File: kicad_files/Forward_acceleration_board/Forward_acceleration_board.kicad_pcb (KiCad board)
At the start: 2 copper layers, 203.2 x 228.6 mm, 0 parts

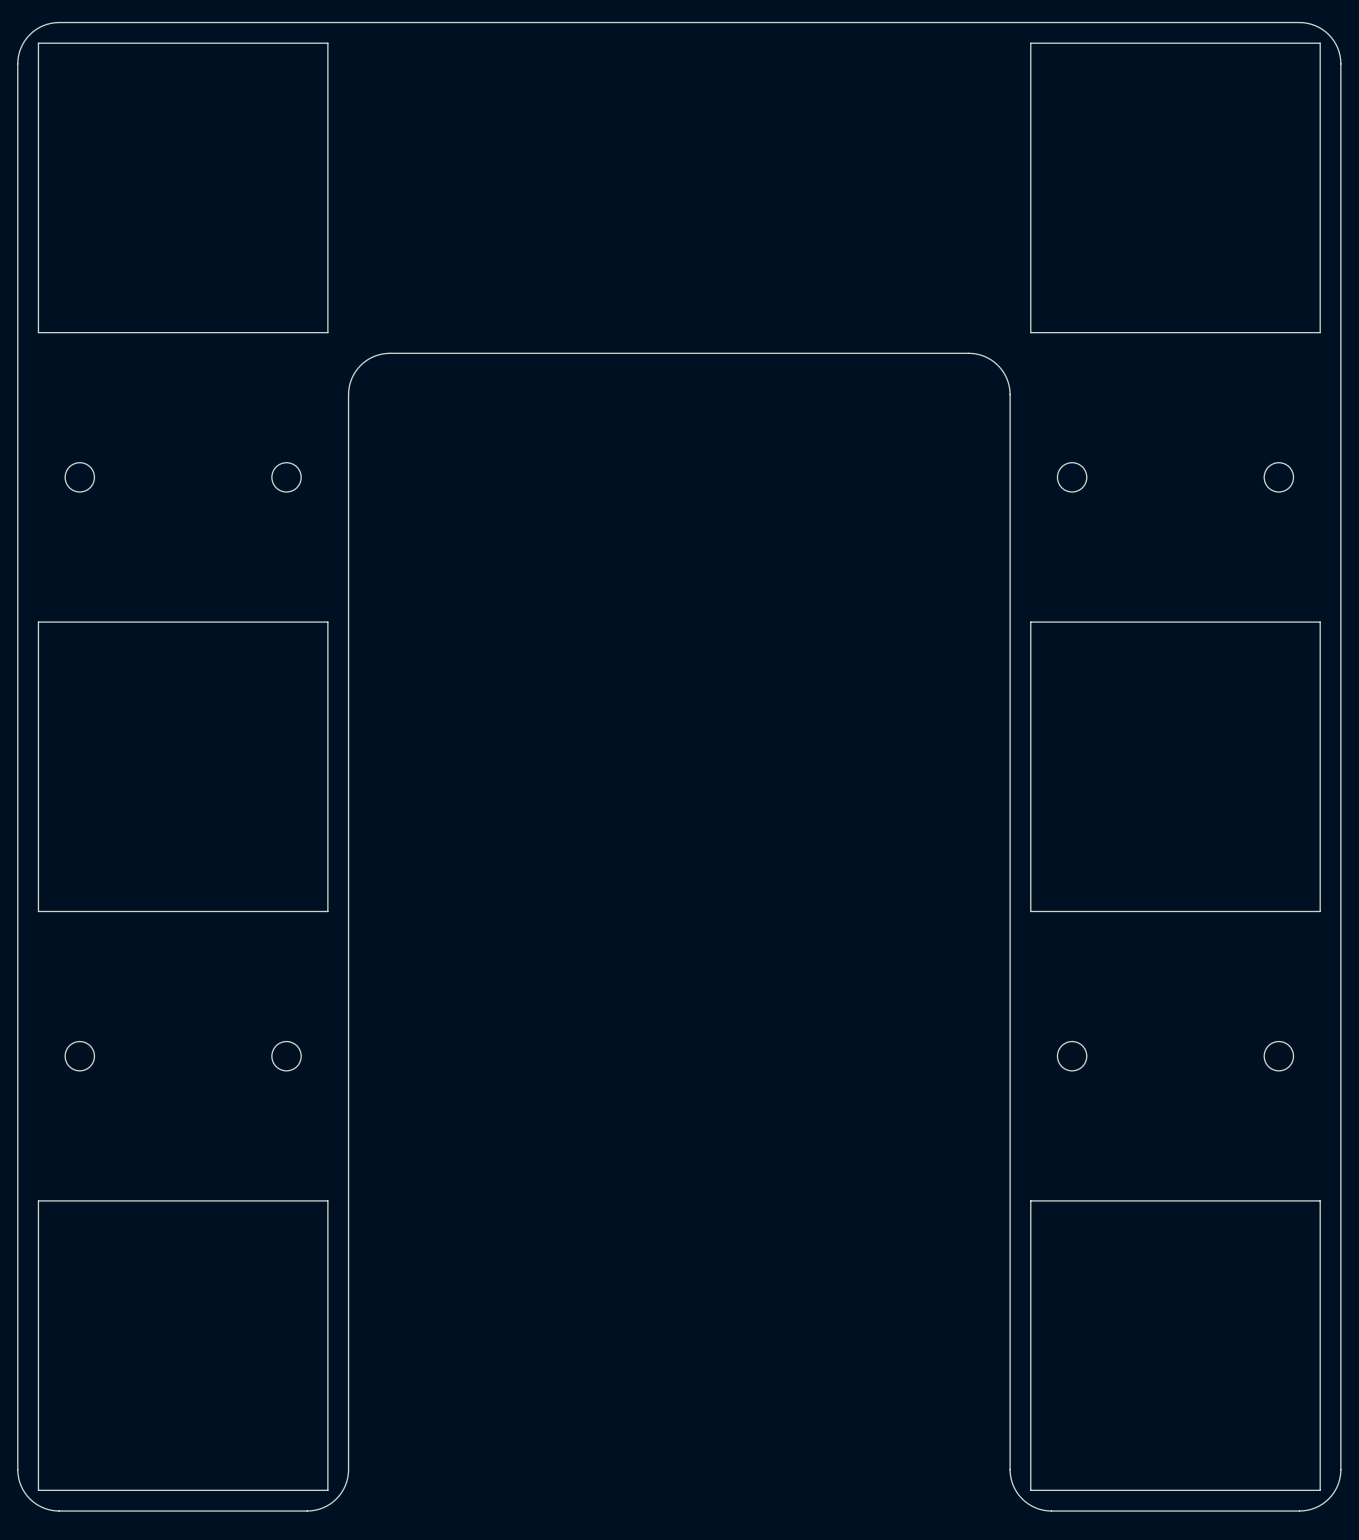
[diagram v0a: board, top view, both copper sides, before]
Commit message: nearly completed forward acceleration control board rounded edges and established clearence for motor control board made progress canabalizing Vedder's code for motor control
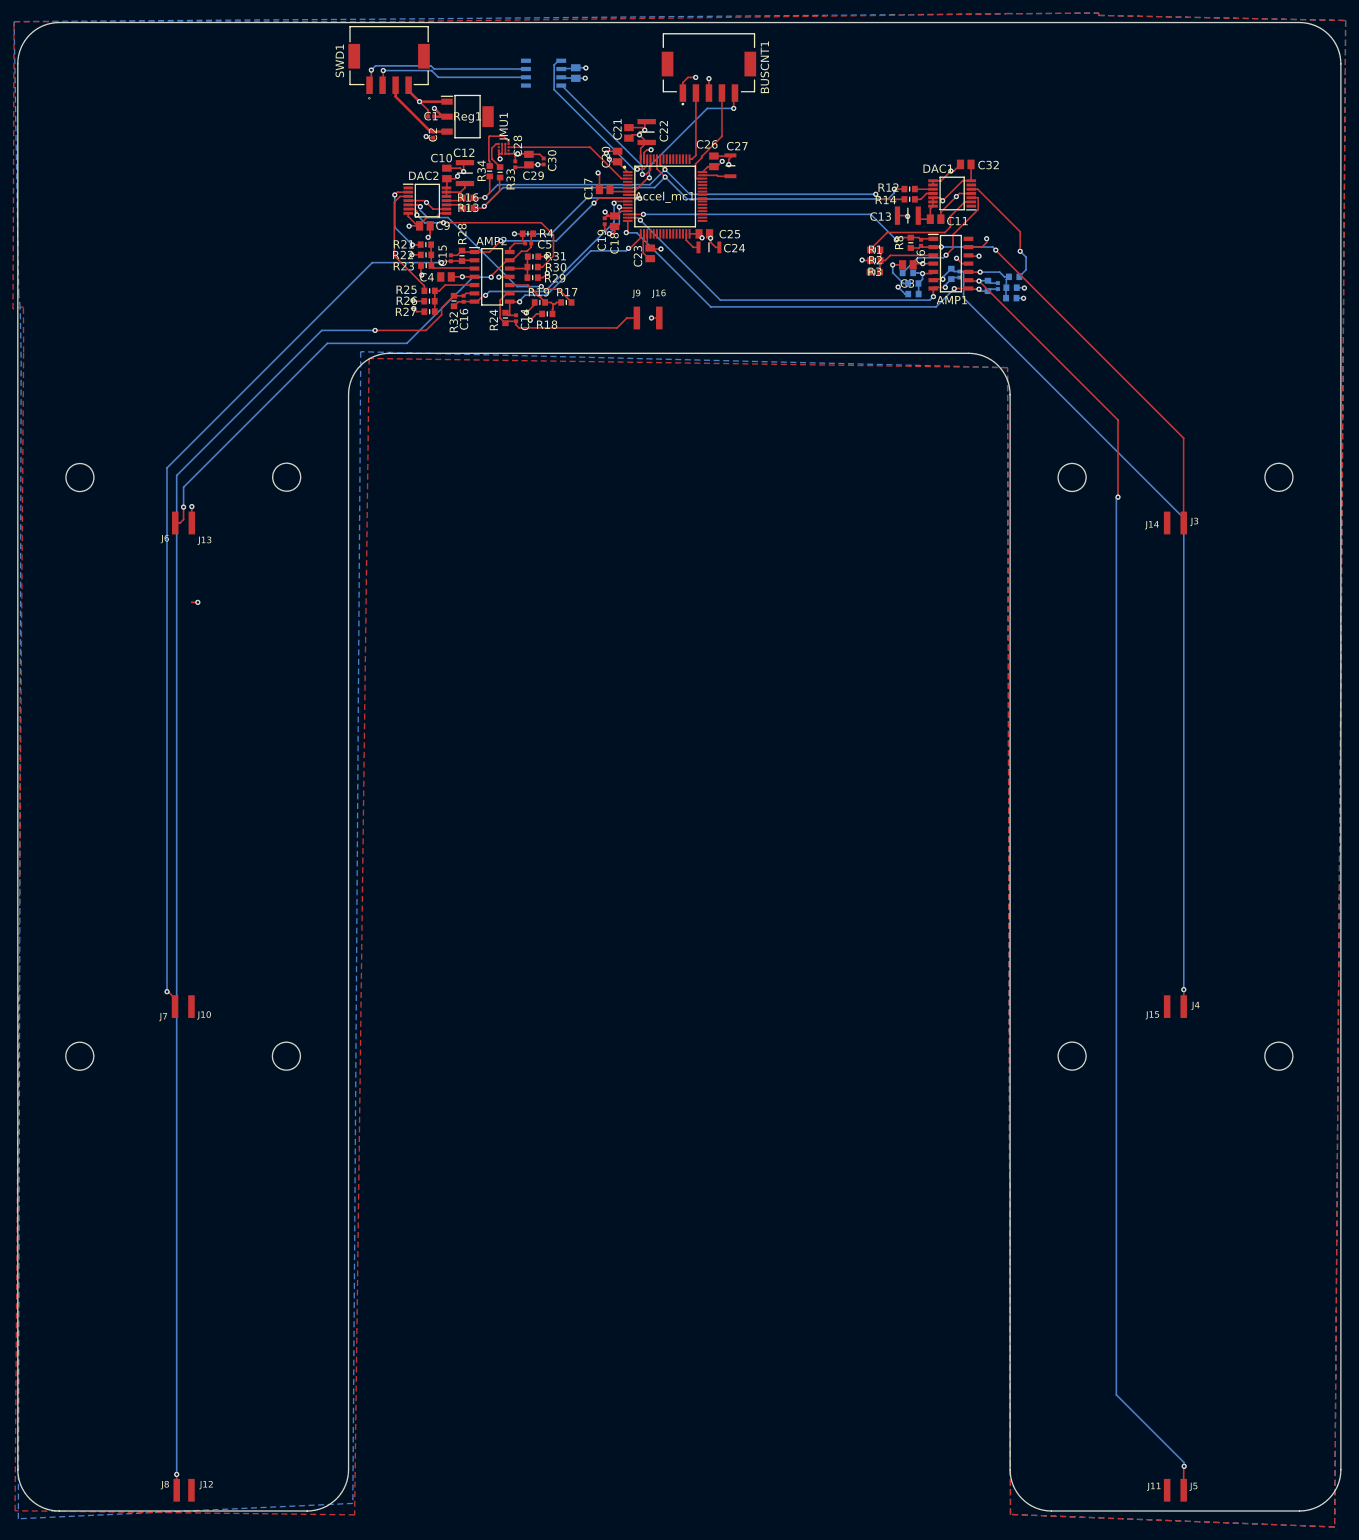
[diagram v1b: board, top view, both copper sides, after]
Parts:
- added AMP1: MCP6054+E_SL, MCP6054-E_SL:SOIC127P600X175-14N, F.Cu at (225.9, 69.3)
- added AMP2: MCP6054+E_SL, MCP6054-E_SL:SOIC127P600X175-14N, F.Cu at (155.4, 71.3)
- added Accel_mc1: STM32F205RBT6, STM32F205RBT6:QFP50P1200X1200X160-64N, F.Cu at (182.0, 59.0)
- added BUSCNT1: SM05B-PASS-TBT(LF)(SN), SM05B-PASS-TBT(LF)(SN):SM05BPASSTBTLFSN, F.Cu at (188.7, 39.5)
- added C1: 1u, GRM155C91C105ME11J:CAPC1005X55N, F.Cu at (146.1, 46.7)
- added C10: .1u, AS0805KKX7R0BB104:CAPC2012X145N, F.Cu at (148.5, 55.5)
- added C11: .1u, AS0805KKX7R0BB104:CAPC2012X145N, F.Cu at (223.5, 62.5)
- added C12: 4.7u, CGA6M3X7S2A475K200AB:CAPC3225X200N, F.Cu at (151.2, 55.4)
- added C13: 4.7u, CGA6M3X7S2A475K200AB:CAPC3225X200N, F.Cu at (219.3, 61.9)
- added C14: 47p, GRM155C91C105ME11J:CAPC1005X55N, F.Cu at (159.1, 77.7)
- added C15: 47p, GRM155C91C105ME11J:CAPC1005X55N, F.Cu at (149.1, 68.5)
- added C16: 47p, GRM155C91C105ME11J:CAPC1005X55N, F.Cu at (151.1, 74.7)
- added C17: .1u, AS0805KKX7R0BB104:CAPC2012X145N, F.Cu at (172.7, 57.9)
- added C18: .1u, AS0805KKX7R0BB104:CAPC2012X145N, F.Cu at (174.2, 62.8)
- added C19: 1u, GRM155C91C105ME11J:CAPC1005X55N, F.Cu at (172.7, 62.8)
- added C2: 1u, GRM155C91C105ME11J:CAPC1005X55N, F.Cu at (146.4, 49.5)
- added C20: .1u, AS0805KKX7R0BB104:CAPC2012X145N, F.Cu at (174.7, 52.9)
- added C21: .1u, AS0805KKX7R0BB104:CAPC2012X145N, F.Cu at (176.4, 49.2)
- added C22: 4.7u, CGA6M3X7S2A475K200AB:CAPC3225X200N, F.Cu at (179.2, 49.1)
- added C23: .1u, AS0805KKX7R0BB104:CAPC2012X145N, F.Cu at (179.7, 67.7)
- added C24: 2.2u, C3216X7R1H225K160AE:CAPC3216X180N, F.Cu at (188.7, 66.8)
- added C25: .1u, AS0805KKX7R0BB104:CAPC2012X145N, F.Cu at (188.0, 64.7)
- added C26: .1u, AS0805KKX7R0BB104:CAPC2012X145N, F.Cu at (189.5, 53.6)
- added C27: 2.2u, C3216X7R1H225K160AE:CAPC3216X180N, F.Cu at (192.0, 54.3)
- added C28: .1u, GRM155C91C105ME11J:CAPC1005X55N, F.Cu at (159.0, 54.0)
- added C29: 10u, AS0805KKX7R0BB104:CAPC2012X145N, F.Cu at (161.1, 53.3)
- added C3: .1u, AS0805KKX7R0BB104:CAPC2012X145N, F.Cu at (219.3, 69.5)
- added C30: .1u, GRM155C91C105ME11J:CAPC1005X55N, F.Cu at (163.3, 53.6)
- added C31: 100n, AS0805KKX7R0BB104:CAPC2012X145N, B.Cu at (168.3, 40.0)
- added C32: .1u, AS0805KKX7R0BB104:CAPC2012X145N, F.Cu at (228.2, 54.1)
- added C4: .1u, AS0805KKX7R0BB104:CAPC2012X145N, F.Cu at (148.3, 71.3)
- added C5: 47p, GRM155C91C105ME11J:CAPC1005X55N, F.Cu at (161.0, 66.2)
- added C6: 47p, GRM155C91C105ME11J:CAPC1005X55N, F.Cu at (221.3, 66.1)
- added C7: 47p, GRM155C91C105ME11J:CAPC1005X55N, B.Cu at (227.2, 71.0)
- added C8: 47p, GRM155C91C105ME11J:CAPC1005X55N, B.Cu at (233.1, 72.8)
- added C9: .1u, AS0805KKX7R0BB104:CAPC2012X145N, F.Cu at (145.1, 63.5)
- added CAN_TR1: SN65HVD232DR, SN65HVD232DR:SOIC127P600X175-8N, B.Cu at (163.3, 40.0)
- added DAC1: MAX5815BAUD+, MAX5815BAUD+:SOP65P640X110-14N, F.Cu at (226.1, 58.5)
- added DAC2: MAX5815BAUD+, MAX5815BAUD+:SOP65P640X110-14N, F.Cu at (145.5, 59.6)
- added IMU1: LIS2DTW12TR, LIS2DTW12TR:IIS2MDCTR, F.Cu at (157.2, 51.7)
- added J10: Conn_01x01_Male, Wire_Pads:SolderWirePad_1x01_SMD_1.27x2.54mm, F.Cu at (109.2, 210.6)
- added J11: Conn_01x01_Male, Wire_Pads:SolderWirePad_1x01_SMD_1.27x2.54mm, F.Cu at (259.1, 257.7)
- added J12: Conn_01x01_Male, Wire_Pads:SolderWirePad_1x01_SMD_1.27x2.54mm, F.Cu at (109.2, 284.8)
- added J13: Conn_01x01_Male, Wire_Pads:SolderWirePad_1x01_SMD_1.27x2.54mm, F.Cu at (109.3, 121.3)
- added J14: Conn_01x01_Male, Wire_Pads:SolderWirePad_1x01_SMD_1.27x2.54mm, F.Cu at (259.1, 109.1)
- added J15: Conn_01x01_Male, Wire_Pads:SolderWirePad_1x01_SMD_1.27x2.54mm, F.Cu at (259.1, 183.4)
- added J16: Conn_01x01_Male, Wire_Pads:SolderWirePad_1x01_SMD_1.27x2.54mm, F.Cu at (181.1, 77.7)
- added J3: Conn_01x01_Male, Wire_Pads:SolderWirePad_1x01_SMD_1.27x2.54mm, F.Cu at (261.6, 109.1)
- added J4: Conn_01x01_Male, Wire_Pads:SolderWirePad_1x01_SMD_1.27x2.54mm, F.Cu at (261.6, 183.4)
- added J5: Conn_01x01_Male, Wire_Pads:SolderWirePad_1x01_SMD_1.27x2.54mm, F.Cu at (261.6, 257.7)
- added J6: Conn_01x01_Male, Wire_Pads:SolderWirePad_1x01_SMD_1.27x2.54mm, F.Cu at (106.8, 121.3)
- added J7: Conn_01x01_Male, Wire_Pads:SolderWirePad_1x01_SMD_1.27x2.54mm, F.Cu at (106.7, 210.5)
- added J8: Conn_01x01_Male, Wire_Pads:SolderWirePad_1x01_SMD_1.27x2.54mm, F.Cu at (67.7, 245.4)
- added J9: Conn_01x01_Male, Wire_Pads:SolderWirePad_1x01_SMD_1.27x2.54mm, F.Cu at (177.7, 77.7)
- added R1: 5k, ERJ3RQF4R7V:RESC1608X55N, F.Cu at (214.3, 67.2)
- added R10: 20k, ERJ3RQF4R7V:RESC1608X55N, B.Cu at (235.2, 74.6)
- added R11: 100k, ERJ3RQF4R7V:RESC1608X55N, B.Cu at (235.2, 73.0)
- added R12: 5k, ERJ3RQF4R7V:RESC1608X55N, F.Cu at (219.6, 57.9)
- added R13: 5k, ERJ3RQF4R7V:RESC1608X55N, F.Cu at (151.8, 60.8)
- added R14: 5k, ERJ3RQF4R7V:RESC1608X55N, F.Cu at (219.6, 59.4)
- added R15: 50k, ERJ3RQF4R7V:RESC1608X55N, B.Cu at (225.9, 70.9)
- added R16: 5k, ERJ3RQF4R7V:RESC1608X55N, F.Cu at (151.7, 59.2)
- added R17: 5k, ERJ3RQF4R7V:RESC1608X55N, F.Cu at (166.8, 75.3)
- added R18: 20k, ERJ3RQF4R7V:RESC1608X55N, F.Cu at (163.9, 77.0)
- added R19: 100k, ERJ3RQF4R7V:RESC1608X55N, F.Cu at (162.8, 75.3)
- added R2: 20k, ERJ3RQF4R7V:RESC1608X55N, F.Cu at (214.3, 68.8)
- added R20: 50k, ERJ3RQF4R7V:RESC1608X55N, B.Cu at (231.6, 72.7)
- added R21: 5k, ERJ3RQF4R7V:RESC1608X55N, F.Cu at (145.2, 66.4)
- added R22: 20k, ERJ3RQF4R7V:RESC1608X55N, F.Cu at (145.3, 68.0)
- added R23: 100k, ERJ3RQF4R7V:RESC1608X55N, F.Cu at (145.3, 69.6)
- added R24: 50k, ERJ3RQF4R7V:RESC1608X55N, F.Cu at (157.5, 77.7)
- added R25: 5k, ERJ3RQF4R7V:RESC1608X55N, F.Cu at (145.8, 73.5)
- added R26: 20k, ERJ3RQF4R7V:RESC1608X55N, F.Cu at (145.8, 75.1)
- added R27: 100k, ERJ3RQF4R7V:RESC1608X55N, F.Cu at (145.8, 76.7)
- added R28: 50k, ERJ3RQF4R7V:RESC1608X55N, F.Cu at (150.8, 68.1)
- added R29: 5k, ERJ3RQF4R7V:RESC1608X55N, F.Cu at (161.7, 71.5)
- added R3: 100k, ERJ3RQF4R7V:RESC1608X55N, F.Cu at (214.2, 70.6)
- added R30: 20k, ERJ3RQF4R7V:RESC1608X55N, F.Cu at (161.7, 69.8)
- added R31: 100k, ERJ3RQF4R7V:RESC1608X55N, F.Cu at (161.7, 68.2)
- added R32: 50k, ERJ3RQF4R7V:RESC1608X55N, F.Cu at (149.6, 75.0)
- added R33: 5k, ERJ3RQF4R7V:RESC1608X55N, F.Cu at (156.7, 55.3)
- added R34: 5k, ERJ3RQF4R7V:RESC1608X55N, F.Cu at (155.1, 55.1)
- added R4: 50k, ERJ3RQF4R7V:RESC1608X55N, F.Cu at (160.9, 64.7)
- added R5: 5k, ERJ3RQF4R7V:RESC1608X55N, B.Cu at (219.3, 70.7)
- added R6: 20k, ERJ3RQF4R7V:RESC1608X55N, B.Cu at (220.1, 74.0)
- added R7: 100k, ERJ3RQF4R7V:RESC1608X55N, B.Cu at (220.1, 72.3)
- added R8: 50k, ERJ3RQF4R7V:RESC1608X55N, F.Cu at (219.7, 66.1)
- added R9: 5k, ERJ3RQF4R7V:RESC1608X55N, B.Cu at (235.6, 71.3)
- added REF**: MountingHole_4.3mm_M4, MountingHole:MountingHole_4.3mm_M4, F.Cu at (276.3, 102.1)
- added REF**: MountingHole_4.3mm_M4, MountingHole:MountingHole_4.3mm_M4, F.Cu at (123.8, 191.0)
- added REF**: MountingHole_4.3mm_M4, MountingHole:MountingHole_4.3mm_M4, F.Cu at (92.1, 102.2)
- added REF**: MountingHole_4.3mm_M4, MountingHole:MountingHole_4.3mm_M4, F.Cu at (244.5, 102.1)
- added REF**: MountingHole_4.3mm_M4, MountingHole:MountingHole_4.3mm_M4, F.Cu at (276.2, 191.0)
- added REF**: MountingHole_4.3mm_M4, MountingHole:MountingHole_4.3mm_M4, F.Cu at (244.5, 191.0)
- added REF**: MountingHole_4.3mm_M4, MountingHole:MountingHole_4.3mm_M4, F.Cu at (92.1, 191.0)
- added REF**: MountingHole_4.3mm_M4, MountingHole:MountingHole_4.3mm_M4, F.Cu at (123.9, 102.1)
- added Reg1: TC2117, TC2117:SOT230P700X180-4N, F.Cu at (151.7, 46.7)
- added SWD1: SM04B-PASS-TBT(LF)(SN), SM04B-PASS-TBT(LF)(SN):SM04B-PASS-TBT, F.Cu at (139.6, 41.8)
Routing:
- net /FSR_Circuitry/-ref6: track 0.00 -> 213.8 mm, vias 0 -> 2
- net /FSR_Circuitry/-ref3: track 0.00 -> 204.0 mm, vias 0 -> 3
- net /FSR_Circuitry/-ref5: track 0.00 -> 143.9 mm, vias 0 -> 2
- net /FSR_Circuitry/-ref2: track 0.00 -> 132.6 mm, vias 0 -> 2
- net GND: track 0.00 -> 110.3 mm, vias 0 -> 32
- net +3V3: track 0.00 -> 102.0 mm, vias 0 -> 23
- net /Controller/SDA: track 0.00 -> 79.4 mm, vias 0 -> 3
- net /FSR_Circuitry/-ref4: track 0.00 -> 77.4 mm, vias 0 -> 2
- net /Controller/SCL: track 0.00 -> 75.7 mm, vias 0 -> 3
- net /FSR_Circuitry/-ref1: track 0.00 -> 67.4 mm, vias 0 -> 2
- net /Controller/Bottom_left_FSR_out: track 0.00 -> 65.2 mm, vias 0 -> 3
- net /FSR_Circuitry/FSR_out2: track 0.00 -> 58.6 mm, vias 0 -> 3
- net /FSR_Circuitry/FSR_out1: track 0.00 -> 49.6 mm, vias 0 -> 2
- net /Controller/Bottom_right_FSR_out: track 0.00 -> 35.1 mm, vias 0 -> 2
- net /FSR_Circuitry/break_DAC: track 0.00 -> 31.7 mm, vias 0 -> 2
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- added copper zone on In1.Cu, net +3V3
- added copper zone on B.Cu, net GND
- added copper zone on F.Cu, net GND
- added copper zone on In2.Cu, net GND
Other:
- outline, holes or cut-outs redrawn
- copper layers 2 -> 4

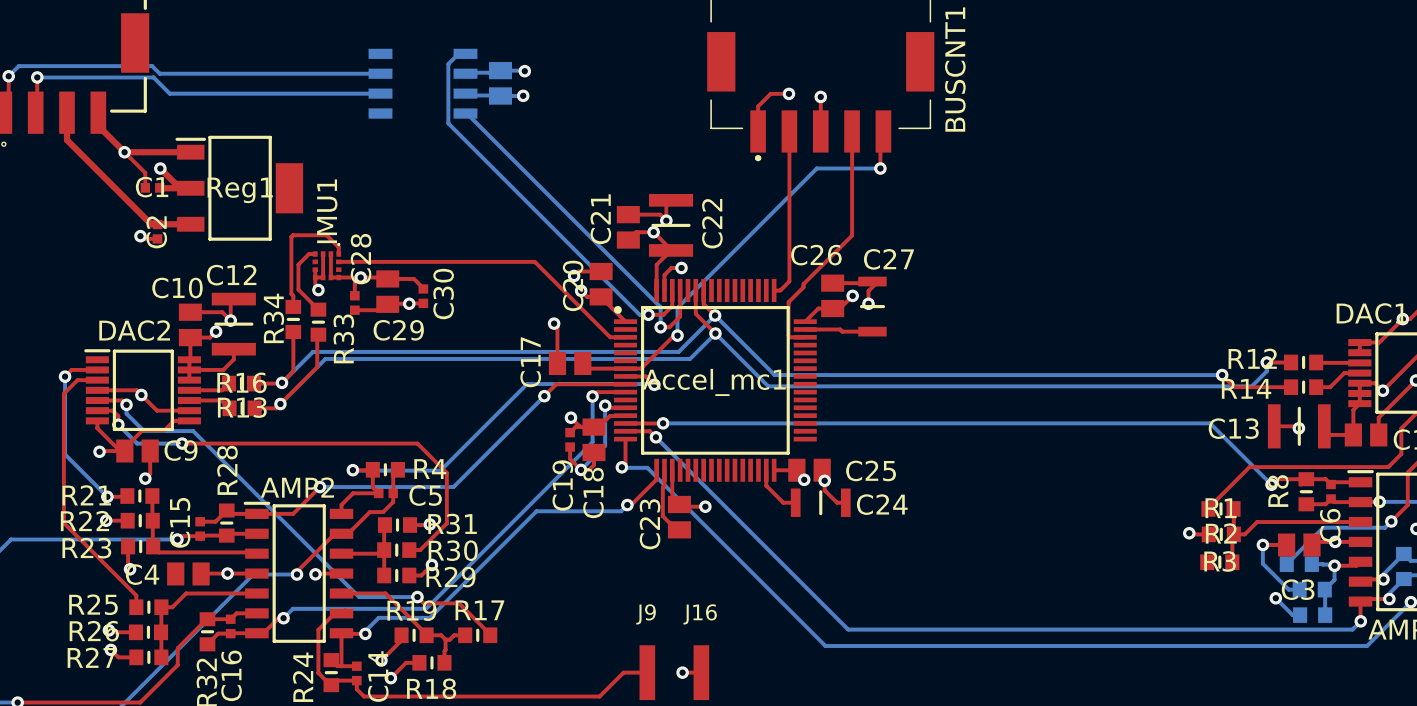
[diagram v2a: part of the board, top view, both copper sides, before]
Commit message: replaced 220nf resistor with component that fit, moved silkscreen around, updated BOM
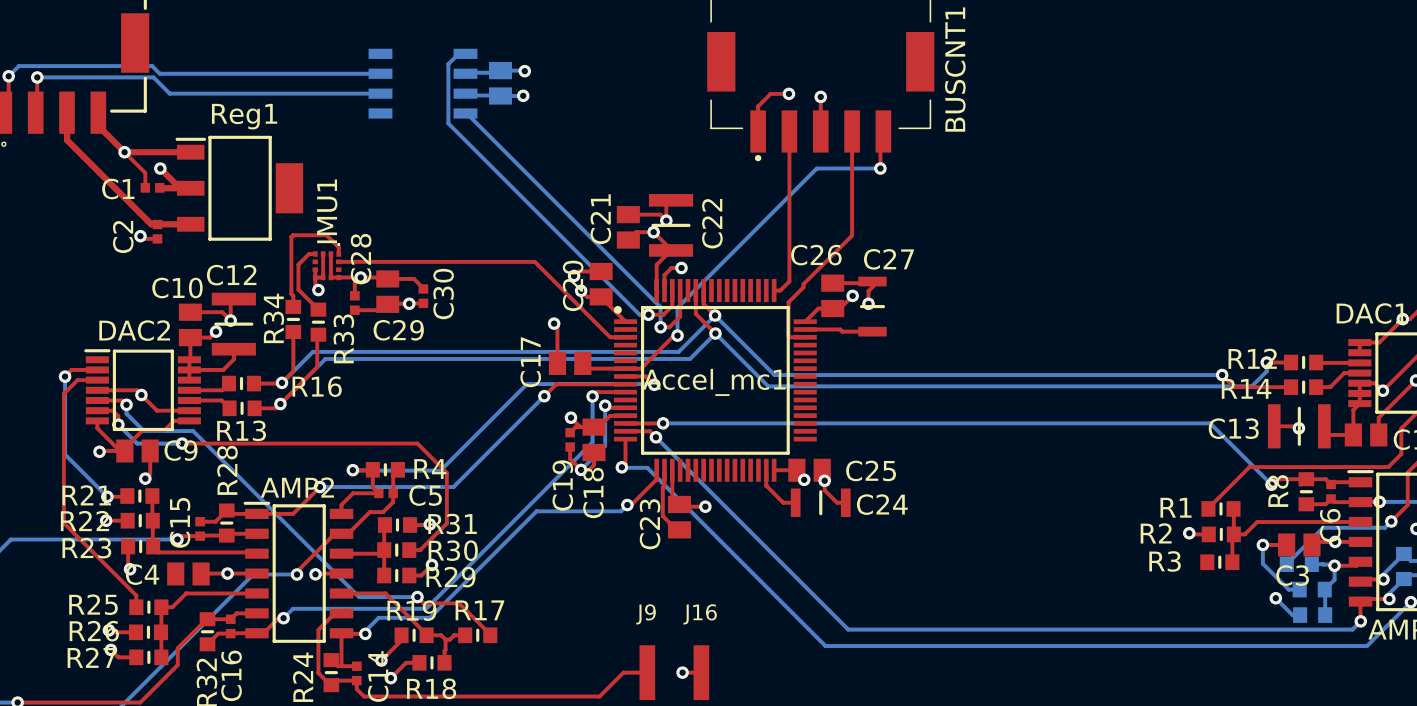
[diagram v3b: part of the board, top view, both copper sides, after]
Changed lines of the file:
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@@
-(kicad_pcb (version 20171130) (host pcbnew 5.1.4-e60b266~84~ubuntu19.04.1)
+(kicad_pcb (version 20171130) (host pcbnew 5.1.4+dfsg1-1)
   (general
     (thickness 1.6)
@@
     (tags Resistor)
     (attr smd)
-    (fp_text reference R2 (at 0 0) (layer F.SilkS)
+    (fp_text reference R2 (at -4.157013 -0.004995) (layer F.SilkS)
       (effects (font (size 1.27 1.27) (thickness 0.254)))
     )
@@
     (tags Resistor)
     (attr smd)
-    (fp_text reference R13 (at 0 0) (layer F.SilkS)
+    (fp_text reference R13 (at -0.047 1.485) (layer F.SilkS)
       (effects (font (size 1.27 1.27) (thickness 0.254)))
     )
@@
     (tags Resistor)
     (attr smd)
-    (fp_text reference R1 (at 0 0) (layer F.SilkS)
+    (fp_text reference R1 (at -2.877 -0.03) (layer F.SilkS)
       (effects (font (size 1.27 1.27) (thickness 0.254)))
     )
@@
     (tags Resistor)
     (attr smd)
-    (fp_text reference R3 (at 0 0) (layer F.SilkS)
+    (fp_text reference R3 (at 3.512 0) (layer F.SilkS)
       (effects (font (size 1.27 1.27) (thickness 0.254)))
     )
@@
     (tags Resistor)
     (attr smd)
-    (fp_text reference R16 (at 0 0) (layer F.SilkS)
+    (fp_text reference R16 (at 4.797989 0.245007) (layer F.SilkS)
       (effects (font (size 1.27 1.27) (thickness 0.254)))
     )
@@
     (tags Capacitor)
     (attr smd)
-    (fp_text reference C2 (at 0 0 90) (layer F.SilkS)
+    (fp_text reference C2 (at 0.3 2.137 90) (layer F.SilkS)
       (effects (font (size 1.27 1.27) (thickness 0.254)))
     )
@@
     (tags Capacitor)
     (attr smd)
-    (fp_text reference C3 (at 0.055 -2.9) (layer F.SilkS)
+    (fp_text reference C3 (at 0.407 -2) (layer F.SilkS)
       (effects (font (size 1.27 1.27) (thickness 0.254)))
     )
@@
     (tags "Power Supply")
     (attr smd)
-    (fp_text reference Reg1 (at 0 0) (layer F.SilkS)
+    (fp_text reference Reg1 (at 0.278 -4.705) (layer F.SilkS)
       (effects (font (size 1.27 1.27) (thickness 0.254)))
     )
@@
     (tags Capacitor)
     (attr smd)
-    (fp_text reference C1 (at 0 0) (layer F.SilkS)
+    (fp_text reference C1 (at 2.152 -0.12) (layer F.SilkS)
       (effects (font (size 1.27 1.27) (thickness 0.254)))
     )
